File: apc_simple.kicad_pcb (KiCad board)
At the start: 2 copper layers, 16 parts, among them J1 Output, J2 Power, U1 NE556

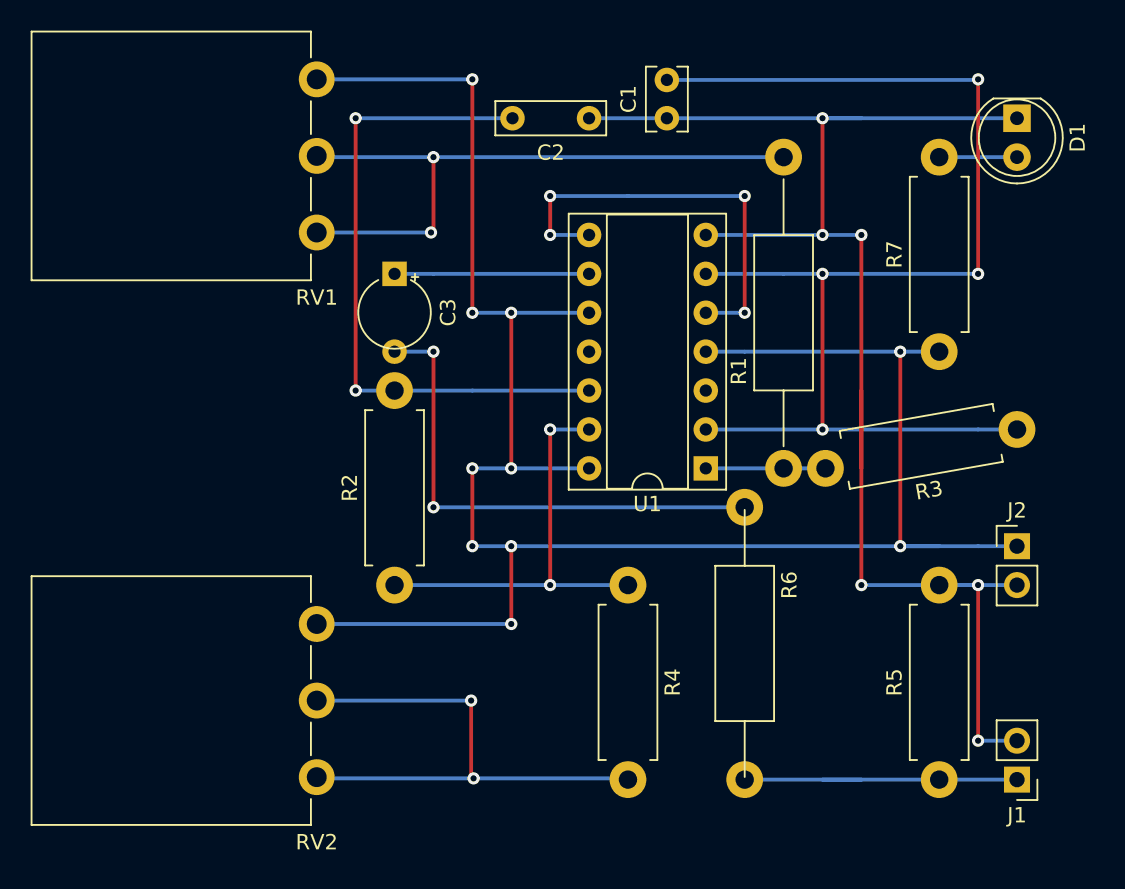
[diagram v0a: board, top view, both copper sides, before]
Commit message: pcb: rearrange cutmarks, add wire shorts
Some places are easier just to short on the backside.
This saves some wire bridges and allows to place cut
indicators a little better aligned.
Also add an 'APC' text by squishing resistors R4 and
R6 a little to the side.
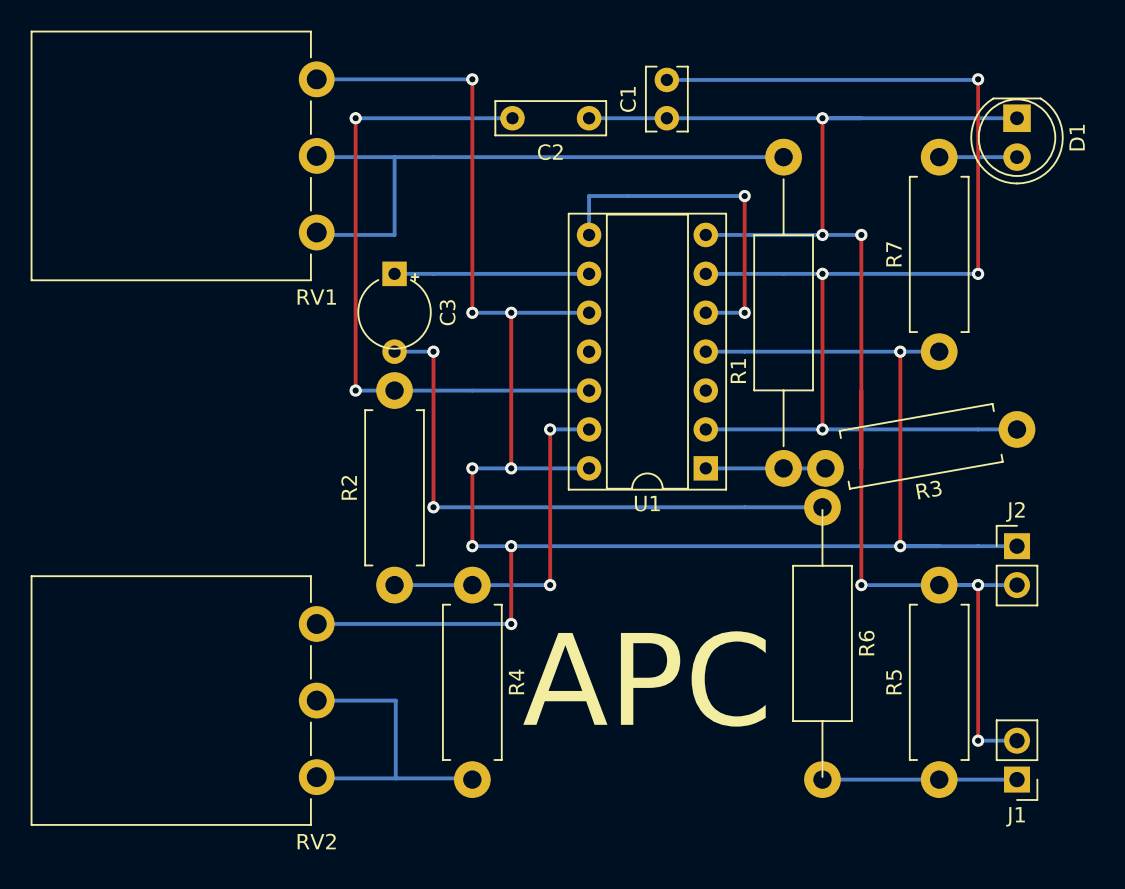
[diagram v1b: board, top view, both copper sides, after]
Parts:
- moved R4 10.2 mm to (124.5, 109.2)
- moved R6 5.08 mm to (147.3, 102.9)
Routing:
- net Net-(R4-Pad2): track 35.6 -> 20.5 mm, vias 2 -> 0
- net Net-(J1-Pad1): track 20.3 -> 12.7 mm
- net Net-(U1-Pad5): track 27.9 -> 22.9 mm, vias 4 -> 2
- net Net-(R2-Pad1): track 27.9 -> 22.9 mm
- net Net-(C3-Pad2): track 33.0 -> 38.1 mm
- net Net-(R1-Pad2): track 42.9 -> 40.6 mm, vias 2 -> 0
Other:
- board text added: "APC"
- board text added: "onsole"
- board text added: "tari"
- board text added: "unk"
